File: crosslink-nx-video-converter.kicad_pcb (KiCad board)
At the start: 2 copper layers, 192 parts, among them J1 WE_68715014522, J2 WE_68715014522, J3 DC_SOCKET, J4 031-70526-21, J5 031-70526-21, U1 AP7330-W5-7, U10 GS2971A, U11 GS2988, U2 AP7330-W5-7, U3 AP7330-W5-7, U4 AP62301WU-7, U5 AP62301WU-7, U6 AP62301WU-7, U7 MT41K128M16JT-125_K, U8 NCV51200MNTXG, U9 LIFCL-40-9BG256C, Y1 ABM7_27.000MH_D2Y_T

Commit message: Made PCB mockup
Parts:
- removed F3, F4, F5: 04671.25NR, antmicro-footprints:0603-Fuse-Littelfuse-0467
- added C100: C_100n_0603, antmicro-footprints:0603-cap, F.Cu at (496.9, 90.8)
- added C101: C_100n_0603, antmicro-footprints:0603-cap, F.Cu at (493.3, 98.2)
- added C102: C_100n_0603, antmicro-footprints:0603-cap, F.Cu at (500.4, 90.8)
- added C103: C_100n_0603, antmicro-footprints:0603-cap, F.Cu at (493.3, 90.8)
- added C104: C_100n_0603, antmicro-footprints:0603-cap, F.Cu at (496.9, 85.8)
- added C105: C_100n_0603, antmicro-footprints:0603-cap, F.Cu at (489.8, 95.7)
- added C106: C_100n_0603, antmicro-footprints:0603-cap, F.Cu at (496.9, 93.2)
- added C94: C_100n_0603, antmicro-footprints:0603-cap, F.Cu at (452.4, 107.2)
- added C99: C_100n_0603, antmicro-footprints:0603-cap, F.Cu at (489.8, 88.3)
- added D1: LTST-C190GKT, antmicro-footprints:LED_0603, F.Cu at (322.0, 107.8)
- added D10: LTST-C190GKT, antmicro-footprints:LED_0603, F.Cu at (167.0, 59.0)
- added D11: LTST-C190GKT, antmicro-footprints:LED_0603, F.Cu at (153.0, 108.5)
- added D12: LTST-C190KRKT, antmicro-footprints:LED_0603, F.Cu at (156.0, 108.5)
- added D2: LTST-C190GKT, antmicro-footprints:LED_0603, F.Cu at (324.0, 107.8)
- added D3: LTST-C190GKT, antmicro-footprints:LED_0603, F.Cu at (326.0, 107.8)
- added D4: LTST-C190GKT, antmicro-footprints:LED_0603, F.Cu at (328.0, 107.8)
- added D5: LTST-C190GKT, antmicro-footprints:LED_0603, F.Cu at (330.0, 107.8)
- added D6: LTST-C190GKT, antmicro-footprints:LED_0603, F.Cu at (332.0, 107.8)
- added D7: LTST-C190GKT, antmicro-footprints:LED_0603, F.Cu at (334.0, 107.8)
- added D8: LTST-C190GKT, antmicro-footprints:LED_0603, F.Cu at (336.0, 107.8)
- added D9: LTST-C190GKT, antmicro-footprints:LED_0603, F.Cu at (164.0, 59.0)
- added G***: antmicro-logo_scaled_20mm, antmicro-footprints:antmicro-logo_scaled_20mm, F.Cu at (97.0, 60.0)
- added J6: FTSH-105-01-F-DV-K, antmicro-footprints:PinHeader_2x5_P1.27_SMD, F.Cu at (143.0, 61.0)
- added J7: FTSH-105-01-L-DV-K, antmicro-footprints:PinHeader_2x5_P1.27_SMD, F.Cu at (130.0, 110.0)
- added J8: 2X05, antmicro-footprints:SHF-105-01-X-D-SM, F.Cu at (143.5, 109.5)
- added Q1: 2N7002, antmicro-footprints:SOT-23-3, F.Cu at (374.3, 79.1)
- added Q10: 2N7002, antmicro-footprints:SOT-23-3, F.Cu at (386.7, 57.3)
- added Q11: 2N7002, antmicro-footprints:SOT-23-3, F.Cu at (391.4, 57.3)
- added Q12: 2N7002, antmicro-footprints:SOT-23-3, F.Cu at (376.7, 67.9)
- added Q13: 2N7002, antmicro-footprints:SOT-23-3, F.Cu at (378.3, 121.1)
- added Q2: AO3401A, antmicro-footprints:SOT-23-3, F.Cu at (369.6, 84.4)
- added Q3: AO3401A, antmicro-footprints:SOT-23-3, F.Cu at (381.4, 67.6)
- added Q4: 2N7002, antmicro-footprints:SOT-23-3, F.Cu at (386.1, 67.2)
- added Q5: 2N7002, antmicro-footprints:SOT-23-3, F.Cu at (391.4, 62.2)
- added Q6: AO3401A, antmicro-footprints:SOT-23-3, F.Cu at (396.1, 57.3)
- added Q7: 2N7002, antmicro-footprints:SOT-23-3, F.Cu at (386.7, 62.2)
- added Q8: 2N7002, antmicro-footprints:SOT-23-3, F.Cu at (381.4, 62.6)
- added Q9: 2N7002, antmicro-footprints:SOT-23-3, F.Cu at (381.4, 72.5)
- added R100: R_0R_0603, antmicro-footprints:0603-res, F.Cu at (412.6, 98.8)
- added R101: R_0R_0603, antmicro-footprints:0603-res, F.Cu at (402.0, 103.7)
- added R102: R_0R_0603, antmicro-footprints:0603-res, F.Cu at (412.6, 96.3)
- added R103: R_0R_0603, antmicro-footprints:0603-res, F.Cu at (394.9, 103.8)
- added R104: R_0R_0603, antmicro-footprints:0603-res, F.Cu at (405.5, 96.3)
- added R105: R_10k_0603, antmicro-footprints:0603-res, F.Cu at (397.6, 106.3)
- added R52: 4x51R_0402_array, antmicro-footprints:R_Array_4x0402, F.Cu at (353.0, 101.0)
- added R53: 4x51R_0402_array, antmicro-footprints:R_Array_4x0402, F.Cu at (353.0, 104.2)
- added R54: R_240R_1%_0402, antmicro-footprints:0402-res, F.Cu at (400.1, 67.7)
- added R55: R_75R_0402, antmicro-footprints:0402-res, F.Cu at (383.1, 85.5)
- added R56: R_75R_0402, antmicro-footprints:0402-res, F.Cu at (382.1, 90.4)
- added R57: R_37R4_0402, antmicro-footprints:0402-res, F.Cu at (393.1, 87.0)
- added R58: R_750R_0603, antmicro-footprints:0603-res, F.Cu at (392.0, 77.2)
- added R59: R_0R_0603, antmicro-footprints:0603-res, F.Cu at (379.1, 79.4)
- added R60: R_100k_0603, antmicro-footprints:0603-res, F.Cu at (407.1, 74.2)
- added R61: R_100k_0603, antmicro-footprints:0603-res, F.Cu at (399.1, 80.0)
- added R62: R_75R_0402, antmicro-footprints:0402-res, F.Cu at (409.1, 61.9)
- added R63: R_75R_0402, antmicro-footprints:0402-res, F.Cu at (400.1, 70.2)
- added R64: R_75R_0402, antmicro-footprints:0402-res, F.Cu at (408.8, 64.3)
- added R65: R_75R_0402, antmicro-footprints:0402-res, F.Cu at (452.7, 105.0)
- added R66: R_105R_0402, antmicro-footprints:0402-res, F.Cu at (449.1, 106.7)
- added R67: R_470R_0603, antmicro-footprints:0603-res, F.Cu at (452.0, 76.4)
- added R68: R_470R_0603, antmicro-footprints:0603-res, F.Cu at (448.5, 76.4)
- added R69: R_0R_0603, antmicro-footprints:0603-res, F.Cu at (389.6, 112.8)
- added R70: R_0R_0603, antmicro-footprints:0603-res, F.Cu at (389.6, 117.7)
- added R71: R_0R_0603, antmicro-footprints:0603-res, F.Cu at (404.7, 106.2)
- added R72: R_0R_0603, antmicro-footprints:0603-res, F.Cu at (386.0, 115.8)
- added R73: R_0R_0603, antmicro-footprints:0603-res, F.Cu at (402.0, 96.3)
- added R74: R_0R_0603, antmicro-footprints:0603-res, F.Cu at (367.5, 125.0)
- added R75: R_10k_0603, antmicro-footprints:0603-res, F.Cu at (396.6, 116.2)
- added R76: R_100R_0603, antmicro-footprints:0603-res, F.Cu at (401.1, 106.3)
- added R77: R_0R_0603, antmicro-footprints:0603-res, F.Cu at (385.9, 120.8)
- added R78: R_100R_0603, antmicro-footprints:0603-res, F.Cu at (409.1, 98.8)
- added R79: R_1k_0603, antmicro-footprints:0603-res, F.Cu at (408.2, 106.2)
- added R80: R_0R_0603, antmicro-footprints:0603-res, F.Cu at (388.4, 123.2)
- added R81: R_0R_0603, antmicro-footprints:0603-res, F.Cu at (396.6, 111.2)
- added R82: R_0R_0603, antmicro-footprints:0603-res, F.Cu at (377.7, 124.8)
- added R83: R_0R_0603, antmicro-footprints:0603-res, F.Cu at (393.1, 115.3)
- added R84: R_0R_0603, antmicro-footprints:0603-res, F.Cu at (402.0, 98.8)
- added R85: R_0R_0603, antmicro-footprints:0603-res, F.Cu at (405.6, 103.7)
- added R86: R_0R_0603, antmicro-footprints:0603-res, F.Cu at (389.6, 115.3)
- added R87: R_0R_0603, antmicro-footprints:0603-res, F.Cu at (409.1, 101.2)
- added R88: R_0R_0603, antmicro-footprints:0603-res, F.Cu at (405.6, 101.2)
- added R89: R_0R_0603, antmicro-footprints:0603-res, F.Cu at (409.1, 96.3)
- added R90: R_4k7_0603, antmicro-footprints:0603-res, F.Cu at (395.0, 108.8)
- added R91: R_10k_0603, antmicro-footprints:0603-res, F.Cu at (393.1, 117.7)
- added R92: R_0R_0603, antmicro-footprints:0603-res, F.Cu at (387.9, 110.3)
- added R93: R_4k7_0603, antmicro-footprints:0603-res, F.Cu at (402.1, 108.8)
- added R94: R_100R_0603, antmicro-footprints:0603-res, F.Cu at (384.8, 124.8)
- added R95: R_4k7_0603, antmicro-footprints:0603-res, F.Cu at (371.1, 125.0)
- added R96: R_2k2_0603, antmicro-footprints:0603-res, F.Cu at (398.5, 103.8)
- added R97: R_10k_0603, antmicro-footprints:0603-res, F.Cu at (416.2, 96.3)
- added R98: R_0R_0603, antmicro-footprints:0603-res, F.Cu at (393.1, 112.8)
- added R99: R_2k2_0603, antmicro-footprints:0603-res, F.Cu at (393.1, 120.2)
- added REF**: mounting-hole-2.7mm-M2.5-Pad, antmicro-footprints:mounting-hole-2.7mm-M2.5-Pad, F.Cu at (80.0, 60.0)
- added REF**: mounting-hole-2.7mm-M2.5-Pad, antmicro-footprints:mounting-hole-2.7mm-M2.5-Pad, F.Cu at (80.0, 110.0)
- added REF**: mounting-hole-2.7mm-M2.5-Pad, antmicro-footprints:mounting-hole-2.7mm-M2.5-Pad, F.Cu at (175.0, 60.0)
- added REF**: mounting-hole-2.7mm-M2.5-Pad, antmicro-footprints:mounting-hole-2.7mm-M2.5-Pad, F.Cu at (175.0, 110.0)
- added S1: B3U-3000PM, antmicro-footprints:B3U-3000P, F.Cu at (154.5, 113.0)
- added SW1: SW_DIP_x06, antmicro-footprints:SW_SPST_6_Slide_MCDHN-06F-T-V_P1.27mm, F.Cu at (156.6, 61.0)
- added TP13: TP, antmicro-footprints:TP-R-1.5, F.Cu at (416.2, 66.4)
- added TP14: TP, antmicro-footprints:TP-R-1.5, F.Cu at (413.7, 69.3)
- added TP15: TP, antmicro-footprints:TP-R-1.5, F.Cu at (444.5, 118.1)
- added TP16: TP, antmicro-footprints:TP-R-1.5, F.Cu at (405.1, 108.7)
- added TP17: TP, antmicro-footprints:TP-R-1.5, F.Cu at (415.7, 98.8)
- added TP18: TP, antmicro-footprints:TP-R-1.5, F.Cu at (399.7, 113.7)
- added TP19: TP, antmicro-footprints:TP-R-1.5, F.Cu at (403.2, 111.2)
- added TP20: TP, antmicro-footprints:TP-R-1.5, F.Cu at (374.2, 113.4)
- added TP21: TP, antmicro-footprints:TP-R-1.5, F.Cu at (412.2, 101.2)
- added TP22: TP, antmicro-footprints:TP-R-1.5, F.Cu at (387.8, 125.7)
- added TP23: TP, antmicro-footprints:TP-R-1.5, F.Cu at (374.1, 125.1)
- added U12: SC18IS602BIPW, antmicro-footprints:SC18IS602B, F.Cu at (128.0, 98.0)
- added U13: W25Q32JVSSIQ, antmicro-footprints:SOIC-8_W5.3mm, F.Cu at (118.0, 98.0)
- added Y2: OSC40M-3.3_S5, antmicro-footprints:OSC-4_5.0x3.2mm, F.Cu at (109.2, 83.5)
- C1, C4: value C_1u_0603 -> C_22u_0805; footprint antmicro-footprints:0603-cap -> antmicro-footprints:0805-cap
- C10, C11, C84, C85: value C_100n_0603 -> C_10u_0603
- C13, C14: value C_22u_0805 -> C_100n_0603; footprint antmicro-footprints:0805-cap -> antmicro-footprints:0603-cap
- C15, C16, C17: value C_22u_0805 -> C_1u_0603; footprint antmicro-footprints:0805-cap -> antmicro-footprints:0603-cap
- C2, C3, C5: value C_1u_0603 -> C_100n_0402; footprint antmicro-footprints:0603-cap -> antmicro-footprints:0402-cap
- C25, C26, C30, C31, C32: value C_100n_0402 -> C_22u_0805; footprint antmicro-footprints:0402-cap -> antmicro-footprints:0805-cap
- C27, C28: value C_100n_0402 -> C_1u_0603; footprint antmicro-footprints:0402-cap -> antmicro-footprints:0603-cap
- C29: value C_100n_0402 -> C_10u_0603; footprint antmicro-footprints:0402-cap -> antmicro-footprints:0603-cap
- C35, C36, C40, C41: value C_22u_0805 -> C_100n_0402; footprint antmicro-footprints:0805-cap -> antmicro-footprints:0402-cap
- C42: value C_100n_0603 -> C_100n_0402; footprint antmicro-footprints:0603-cap -> antmicro-footprints:0402-cap
- C43, C44: value C_100n_0603 -> C_33p_0603
- C45, C46, C49: value C_100n_0603 -> C_1u_0402; footprint antmicro-footprints:0603-cap -> antmicro-footprints:0402-cap
- C47: value C_100n_0603 -> C_47n_0603
- C48, C50: value C_100n_0603 -> C_470n_0603
- C51: value C_100n_0603 -> C_10n_0402; footprint antmicro-footprints:0603-cap -> antmicro-footprints:0402-cap
- C52, C53: value C_100n_0603 -> C_4u7_0402; footprint antmicro-footprints:0603-cap -> antmicro-footprints:0402-cap
- C56, C57, C58, C59, C60, C62: value C_10u_0603 -> C_100n_0603
- C6, C7: value C_10u_0603 -> C_22u_0805; footprint antmicro-footprints:0603-cap -> antmicro-footprints:0805-cap
- C61: value C_1u_0603 -> C_100n_0603
- C63: value C_100n_0603 -> C_33u_0603
- C71, C72: value C_1u_0402 -> C_100n_0603; footprint antmicro-footprints:0402-cap -> antmicro-footprints:0603-cap
- C86: value C_10n_0402 -> C_10u_0603; footprint antmicro-footprints:0402-cap -> antmicro-footprints:0603-cap
- C87, C88: value C_4u7_0402 -> C_10u_0603; footprint antmicro-footprints:0402-cap -> antmicro-footprints:0603-cap
- C89: value C_33p_0603 -> C_1u_0603
- C90: value C_33p_0603 -> C_10u_0603
- C91, C93: value C_470n_0603 -> C_100n_0603
- C92: value C_47n_0603 -> C_100n_0603
- C95: value C_33u_0603 -> C_100n_0603
- J1: value WE_68715014522 -> DC_SOCKET; footprint antmicro-footprints:WE_68715014522 -> antmicro-footprints:DC_SOCKET
- J2: value WE_68715014522 -> 031-70526-21; footprint antmicro-footprints:WE_68715014522 -> antmicro-footprints:BNC_Edge_Conn
- J3: value DC_SOCKET -> 031-70526-21; footprint antmicro-footprints:DC_SOCKET -> antmicro-footprints:BNC_Edge_Conn
- J4, J5: value 031-70526-21 -> WE_68715014522_ONE-SIDE; footprint antmicro-footprints:BNC_Edge_Conn -> antmicro-footprints:WE_68715014522_ONE-SIDE
- R1, R2: value R_0R_0603 -> R_0R_0805; footprint antmicro-footprints:0603-res -> antmicro-footprints:0805-res
- R10: value R_0R_0603 -> R_470R_0603
- R11: value R_0R_0603 -> R_10k_0603
- R12: value R_0R_0603 -> R_100k_0603
- R13, R15: value R_0R_0805 -> R_470R_0603; footprint antmicro-footprints:0805-res -> antmicro-footprints:0603-res
- R16: value R_33k_0603 -> R_470R_0603
- R17: value R_10k_0603 -> R_470R_0603
- R18: value R_3k01_1%_0603 -> R_470R_0603
- R19: value R_10k_1%_0603 -> R_470R_0603
- R20: value R_13k7_1%_0603 -> R_0R_0805; footprint antmicro-footprints:0603-res -> antmicro-footprints:0805-res
- R21: value R_20k_1%_0603 -> R_0R_0805; footprint antmicro-footprints:0603-res -> antmicro-footprints:0805-res
- R23, R24, R33, R34: value R_0R_0805 -> R_0R_0603; footprint antmicro-footprints:0805-res -> antmicro-footprints:0603-res
- R25: value R_100R_0402 -> R_0R_0603; footprint antmicro-footprints:0402-res -> antmicro-footprints:0603-res
- R26: value 4x51R_0402_array -> R_3k01_1%_0603; footprint antmicro-footprints:R_Array_4x0402 -> antmicro-footprints:0603-res
- R27: value 4x51R_0402_array -> R_10k_1%_0603; footprint antmicro-footprints:R_Array_4x0402 -> antmicro-footprints:0603-res
- R28: value 4x51R_0402_array -> R_13k7_1%_0603; footprint antmicro-footprints:R_Array_4x0402 -> antmicro-footprints:0603-res
- R29: value 4x51R_0402_array -> R_20k_1%_0603; footprint antmicro-footprints:R_Array_4x0402 -> antmicro-footprints:0603-res
- R3: value R_0R_0603 -> R_10k_1%_0603
- R30: value 4x51R_0402_array -> R_33k_0603; footprint antmicro-footprints:R_Array_4x0402 -> antmicro-footprints:0603-res
- R31: value 4x51R_0402_array -> R_10k_0603; footprint antmicro-footprints:R_Array_4x0402 -> antmicro-footprints:0603-res
- R32: value R_240R_1%_0402 -> R_0R_0603; footprint antmicro-footprints:0402-res -> antmicro-footprints:0603-res
- R35: value R_10k_1%_0603 -> R_3k01_1%_0603
- R37: value R_100k_0603 -> R_12k_0603
- R38: value R_0R_0603 -> R_24k_0603
- R39: value R_0R_0603 -> R_18k7_1%_0603
- R4: value R_3k01_1%_0603 -> R_10k_1%_0603
- R40: value R_0R_0603 -> R_15k_0603
- R42, R43: value R_75R_0402 -> R_0R_0603; footprint antmicro-footprints:0402-res -> antmicro-footprints:0603-res
- R44: value R_37R4_0402 -> R_0R_0805; footprint antmicro-footprints:0402-res -> antmicro-footprints:0805-res
- R45, R46: value R_75R_0402 -> R_0R_0805; footprint antmicro-footprints:0402-res -> antmicro-footprints:0805-res
- R47: value R_75R_0402 -> R_100R_0402
- R48: value R_75R_0402 -> 4x51R_0402_array; footprint antmicro-footprints:0402-res -> antmicro-footprints:R_Array_4x0402
- R49, R50: value R_100k_0603 -> 4x51R_0402_array; footprint antmicro-footprints:0603-res -> antmicro-footprints:R_Array_4x0402
- R5: value R_10k_1%_0603 -> R_100k_0603
- R51: value R_105R_0402 -> 4x51R_0402_array; footprint antmicro-footprints:0402-res -> antmicro-footprints:R_Array_4x0402
- R6: value R_12k_0603 -> R_0R_0805; footprint antmicro-footprints:0603-res -> antmicro-footprints:0805-res
- R7: value R_24k_0603 -> R_10k_0603
- R8: value R_18k7_1%_0603 -> R_470R_0603
- R9: value R_15k_0603 -> R_0R_0603
- U1: value AP7330-W5-7 -> NCV51200MNTXG; footprint antmicro-footprints:SOT-23-5 -> antmicro-footprints:DFN-10-1EP_3x3mm
- U11: value GS2988 -> LIFCL-40-9BG256C; footprint antmicro-footprints:QFN-16_EP_4x4_Pitch0.65mm -> antmicro-footprints:BGA-256_16x16_14.0x14.0mm
- U2, U3: value AP7330-W5-7 -> AP62301WU-7; footprint antmicro-footprints:SOT-23-5 -> antmicro-footprints:TSOT23-6
- U5, U6: value AP62301WU-7 -> AP7330-W5-7; footprint antmicro-footprints:TSOT23-6 -> antmicro-footprints:SOT-23-5
- U7: value MT41K128M16JT-125_K -> AP7330-W5-7; footprint antmicro-footprints:BGA80P96C6X16_800X1400X110 -> antmicro-footprints:SOT-23-5
- U8: value NCV51200MNTXG -> MT41K128M16JT-125_K; footprint antmicro-footprints:DFN-10-1EP_3x3mm -> antmicro-footprints:BGA80P96C6X16_800X1400X110
- U9: value LIFCL-40-9BG256C -> GS2988; footprint antmicro-footprints:BGA-256_16x16_14.0x14.0mm -> antmicro-footprints:QFN-16_EP_4x4_Pitch0.65mm
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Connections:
- C1 pad 1: +3V3 -> Net-(C1-Pad1)
- C10 pad 2: Net-(C10-Pad2) -> GND
- C11 pad 2: Net-(C11-Pad2) -> GND
- C13 pad 2: GND -> Net-(C13-Pad2)
- C14 pad 2: GND -> Net-(C14-Pad2)
- C15 pad 1: Net-(C15-Pad1) -> +3V3
- C16 pad 1: Net-(C14-Pad1) -> +3V3
- C17 pad 1: Net-(C15-Pad1) -> +3V3
- C18 pad 1: Net-(C13-Pad1) -> Net-(C18-Pad1)
- C19 pad 1: Net-(C14-Pad1) -> Net-(C19-Pad1)
- C2 pad 1: +3V3 -> Net-(C1-Pad1)
- C2 pad 2: GND -> Net-(C2-Pad2)
- C20 pad 1: Net-(C15-Pad1) -> Net-(C20-Pad1)
- C21 pad 1: Net-(C13-Pad1) -> Net-(C18-Pad1)
- C22 pad 1: Net-(C13-Pad1) -> Net-(C19-Pad1)
- C23 pad 1: Net-(C14-Pad1) -> Net-(C20-Pad1)
- C24 pad 1: Net-(C15-Pad1) -> Net-(C18-Pad1)
- C25 pad 1: +1V35 -> Net-(C19-Pad1)
- C26 pad 1: +1V35 -> Net-(C20-Pad1)
- C27 pad 1: +1V35 -> 1V0_Clean
- C28 pad 1: +1V35 -> +1V2
- C29 pad 1: +1V35 -> +1V8
- C3 pad 1: +3V3 -> Net-(C2-Pad2)
- C30 pad 1: +1V35 -> Net-(C18-Pad1)
- C31 pad 1: +1V35 -> Net-(C19-Pad1)
- C32 pad 1: +1V35 -> Net-(C20-Pad1)
- C33 pad 2: Vref -> GND
- C34 pad 1: Vref -> +1V35
- C35 pad 1: Net-(C35-Pad1) -> +1V35
- C36 pad 1: Net-(C36-Pad1) -> +1V35
- C37 pad 1: Net-(C35-Pad1) -> +1V35
- C37 pad 2: Net-(C37-Pad2) -> GND
- C38 pad 1: Net-(C37-Pad2) -> +1V35
- C39 pad 1: Vref -> +1V35
- C4 pad 1: 1V0_Clean -> Net-(C4-Pad1)
- C40 pad 1: Vtt -> +1V35
- C41 pad 1: Vtt -> +1V35
- C41 pad 2: GND -> Vref
- C42 pad 1: +1V35 -> Vref
- C42 pad 2: Vref -> GND
- C43 pad 1: Vref -> GND
- C43 pad 2: GND -> /SDI/XTAL1
- C44 pad 1: +1V35 -> GND
- C44 pad 2: Vref -> /SDI/XTAL2
- C45 pad 1: Vref -> Net-(C45-Pad1)
- C45 pad 2: GND -> /SDI/SDI_P
- C46 pad 1: +1V35 -> Net-(C46-Pad1)
- C46 pad 2: GND -> /SDI/SDI_N
- C47 pad 1: /FPGA/VCC_AUX -> Net-(C47-Pad1)
- C48 pad 1: /FPGA/VCC_AUX -> Net-(C48-Pad1)
- C49 pad 1: 1V0_Power -> GND
- C49 pad 2: GND -> Net-(C49-Pad2)
- C5 pad 1: +1V2 -> Vref
- C50 pad 1: /FPGA/VCC_AUX -> Net-(C48-Pad1)
- C50 pad 2: GND -> Net-(C50-Pad2)
- C51 pad 1: 1V0_Power -> GND
- C51 pad 2: GND -> +3V3
- C52 pad 1: /FPGA/VCC_AUX -> Net-(C52-Pad1)
- C52 pad 2: GND -> Net-(C52-Pad2)
- C53 pad 1: 1V0_Power -> Net-(C53-Pad1)
- C53 pad 2: GND -> Net-(C53-Pad2)
- C54 pad 1: /FPGA/VCC_AUX -> +3V3
- C55 pad 1: +1V35 -> +1V2
- C56 pad 1: 1V0_Power -> +3V3
- C57 pad 1: /FPGA/VCC_AUX -> +1V2
- C58 pad 1: /FPGA/VCC_AUXA -> +3V3
- C59 pad 1: /FPGA/VCC_DPHY -> +1V2
- C6 pad 1: +1V8 -> Vtt
- C60 pad 1: /FPGA/VCC_ADPHY -> +3V3
- C61 pad 1: /FPGA/VCC_PLLDPHY -> +1V2
- C62 pad 1: /FPGA/VCC_AUX -> +3V3
- C63 pad 1: /FPGA/VCC_AUXA -> Net-(C63-Pad1)
- C64 pad 1: /FPGA/VCC_DPHY -> +1V2
- C65 pad 1: /FPGA/VCC_ADPHY -> +3V3
- C66 pad 1: /FPGA/VCC_PLLDPHY -> +1V2
- C67 pad 1: /FPGA/VCC_AUXA -> +3V3
- C68 pad 1: /FPGA/VCC_DPHY -> +1V35
- C68 pad 2: GND -> Vref
- C69 pad 1: /FPGA/VCC_ADPHY -> Vref
- C7 pad 1: Net-(C7-Pad1) -> Vtt
- C70 pad 1: /FPGA/VCC_PLLDPHY -> +3V3
- C71 pad 1: Net-(C71-Pad1) -> +3V3
- C71 pad 2: /SDI/SDI_P -> GND
- C72 pad 1: Net-(C72-Pad1) -> +3V3
- C72 pad 2: /SDI/SDI_N -> GND
- C73 pad 1: +3V3 -> +1V35
- C74 pad 1: +1V2 -> +3V3
- C75 pad 1: +3V3 -> +1V2
- C76 pad 1: +1V2 -> +3V3
- C77 pad 1: +3V3 -> +1V35
- C78 pad 1: +1V2 -> +1V35
- C78 pad 2: GND -> Vref
- C79 pad 1: +3V3 -> Vref
- C8 pad 1: Net-(C8-Pad1) -> +5V
- C80 pad 1: +1V2 -> +3V3
- C81 pad 1: +3V3 -> Net-(C81-Pad1)
- C82 pad 1: +1V2 -> +3V3
- C84 pad 1: +1V2 -> 1V0_Power
- C85 pad 1: +3V3 -> /FPGA Power/VCC_AUX
- C86 pad 1: GND -> /FPGA Power/VCC_AUXA
- C86 pad 2: +3V3 -> GND
- C87 pad 1: Net-(C87-Pad1) -> /FPGA Power/VCC_DPHY
- C87 pad 2: Net-(C87-Pad2) -> GND
- C88 pad 1: Net-(C88-Pad1) -> /FPGA Power/VCC_ADPHY
- C88 pad 2: Net-(C88-Pad2) -> GND
- C89 pad 1: GND -> /FPGA Power/VCC_PLLDPHY
- C89 pad 2: /SDI/XTAL1 -> GND
- C90 pad 1: GND -> /FPGA Power/VCC_AUX
- C90 pad 2: /SDI/XTAL2 -> GND
- C91 pad 1: Net-(U10-PadG1) -> 1V0_Power
- C92 pad 1: Net-(U10-PadA2) -> /FPGA Power/VCC_AUX
- C93 pad 1: Net-(U10-PadG1) -> /FPGA Power/VCC_AUXA
- C93 pad 2: Net-(U10-PadF1) -> GND
- C95 pad 1: Net-(U10-PadA4) -> /FPGA Power/VCC_ADPHY
- C96 pad 1: +3V3 -> /FPGA Power/VCC_PLLDPHY
- C97 pad 1: +3V3 -> 1V0_Power
- C98 pad 1: +1V2 -> /FPGA Power/VCC_AUX
- F1 pad 1: Net-(F1-Pad1) -> /Peripherals/FFC1_5V
- F2 pad 1: +5V -> /Peripherals/FFC1_3V3
- F2 pad 2: Net-(J1-Pad49) -> +3V3
- FB1 pad 1: /FPGA/VCC_AUX -> /FPGA Power/VCC_AUX
- FB2 pad 1: /FPGA/VCC_AUXA -> /FPGA Power/VCC_AUXA
- FB3 pad 1: /FPGA/VCC_DPHY -> /FPGA Power/VCC_DPHY
- FB4 pad 1: /FPGA/VCC_ADPHY -> /FPGA Power/VCC_ADPHY
- FB5 pad 1: /FPGA/VCC_PLLDPHY -> /FPGA Power/VCC_PLLDPHY
- J1 pad 1: MIPI0_D3_N -> ALT_5V
- J1 pad 2: MIPI0_D3_P -> GND
- J1 pad 3: MIPI0_D2_N -> GND
- J2 pad 1: unconnected-(J2-Pad1) -> Net-(J2-Pad1)
- J2 pad 2: unconnected-(J2-Pad2) -> GND
- J3 pad 1: Net-(F1-Pad1) -> Net-(C53-Pad2)
- J4 pad 1: Net-(J4-Pad1) -> MIPI0_D3_N
- J4 pad 2: GND -> MIPI0_D3_P
- J5 pad 1: Net-(C88-Pad2) -> unconnected-(J5-Pad1)
- J5 pad 2: GND -> unconnected-(J5-Pad2)
- L1 pad 1: Net-(C11-Pad2) -> Net-(C12-Pad2)
- L1 pad 2: Net-(C14-Pad1) -> Net-(C18-Pad1)
- L2 pad 1: Net-(C12-Pad2) -> Net-(C13-Pad2)
- L2 pad 2: Net-(C15-Pad1) -> Net-(C19-Pad1)
- L3 pad 1: Net-(C10-Pad2) -> Net-(C14-Pad2)
- L3 pad 2: Net-(C13-Pad1) -> Net-(C20-Pad1)
- L4 pad 1: Net-(C71-Pad1) -> Net-(C45-Pad1)
- L4 pad 2: Net-(J4-Pad1) -> Net-(J2-Pad1)
- L5 pad 1: Net-(L5-Pad1) -> Net-(C53-Pad1)
- L5 pad 2: Net-(C88-Pad1) -> Net-(L5-Pad2)
- R1 pad 1: +3V3 -> +1V35
- R1 pad 2: Net-(R1-Pad2) -> Net-(C1-Pad1)
- R10 pad 1: Net-(R10-Pad1) -> Net-(D2-Pad1)
- R10 pad 2: 1V0_Clean -> +5V
- R11 pad 1: Net-(R11-Pad1) -> Net-(Q3-Pad1)
- R11 pad 2: +1V2 -> Net-(Q3-Pad2)
- R12 pad 1: Net-(R12-Pad1) -> /Power Supply/Vtt_PGOOD
- R12 pad 2: +1V8 -> Net-(C4-Pad1)
- R13 pad 1: +5V -> Net-(D3-Pad1)
- R13 pad 2: Net-(C7-Pad1) -> +5V
- R14 pad 1: +5V -> Net-(Q2-Pad2)
- R14 pad 2: Net-(C8-Pad1) -> +5V
- R15 pad 1: +5V -> Net-(D4-Pad1)
- R15 pad 2: Net-(C9-Pad1) -> +5V
- R16 pad 1: Net-(C13-Pad1) -> Net-(D5-Pad1)
- R16 pad 2: Net-(R16-Pad2) -> +5V
- R17 pad 1: GND -> Net-(D6-Pad1)
- R17 pad 2: Net-(R16-Pad2) -> +5V
- R18 pad 1: Net-(C14-Pad1) -> Net-(D7-Pad1)
- R18 pad 2: Net-(R18-Pad2) -> +5V
- R19 pad 1: Net-(R18-Pad2) -> Net-(D8-Pad1)
- R19 pad 2: GND -> +5V
- R2 pad 1: +3V3 -> FFC2_5V
- R2 pad 2: Net-(R2-Pad2) -> Net-(Q3-Pad3)
- R20 pad 1: Net-(R20-Pad1) -> +5V
- R20 pad 2: Net-(C15-Pad1) -> Net-(C9-Pad1)
- R21 pad 1: GND -> +5V
- R21 pad 2: Net-(R20-Pad1) -> Net-(C10-Pad1)
- R22 pad 1: Net-(C13-Pad1) -> +5V
- R22 pad 2: +3V3 -> Net-(C11-Pad1)
- R23 pad 1: Net-(C14-Pad1) -> +3V3
- R23 pad 2: 1V0_Power -> Net-(R23-Pad2)
- R24 pad 1: Net-(C15-Pad1) -> +3V3
- R24 pad 2: +1V35 -> Net-(R24-Pad2)
- R25 pad 1: DDR3_CK_N -> +3V3
- R25 pad 2: DDR3_CK_P -> Net-(R25-Pad2)
- R26 pad 1: DDR3_A0 -> Net-(C18-Pad1)
- R26 pad 2: DDR3_A1 -> Net-(R26-Pad2)
- R27 pad 1: DDR3_A4 -> Net-(R26-Pad2)
- R27 pad 2: DDR3_A5 -> GND
- R28 pad 1: DDR3_A8 -> Net-(R28-Pad1)
- R28 pad 2: DDR3_A9 -> Net-(C19-Pad1)
- R29 pad 1: DDR3_A12 -> GND
- R29 pad 2: DDR3_A13 -> Net-(R28-Pad1)
- R3 pad 1: +3V3 -> Net-(C2-Pad2)
- R3 pad 2: Net-(R3-Pad2) -> Net-(C1-Pad1)
- R30 pad 1: ~{DDR3_RESET} -> Net-(C20-Pad1)
- R30 pad 2: ~{DDR3_RAS} -> Net-(R30-Pad2)
- R31 pad 1: ~{DDR3_CS} -> GND
- R31 pad 2: DDR3_ODT -> Net-(R30-Pad2)
- R32 pad 1: GND -> Net-(R23-Pad2)
- R33 pad 1: +1V35 -> Net-(R24-Pad2)
- R33 pad 2: Net-(C35-Pad1) -> Net-(R33-Pad2)
- R34 pad 1: +3V3 -> Net-(R25-Pad2)
- R34 pad 2: Net-(C36-Pad1) -> Net-(R34-Pad2)
- R35 pad 1: Net-(C37-Pad2) -> Net-(R35-Pad1)
- R35 pad 2: Net-(C35-Pad1) -> Net-(R35-Pad2)
- R36 pad 1: GND -> Net-(R35-Pad2)
- R36 pad 2: Net-(C37-Pad2) -> GND
- R37 pad 2: Net-(C36-Pad1) -> Net-(R37-Pad2)
- R38 pad 1: Net-(C35-Pad1) -> GND
- R38 pad 2: Net-(U8-Pad7) -> Net-(R37-Pad2)
- R39 pad 1: Net-(R1-Pad2) -> Net-(R39-Pad1)
- R39 pad 2: Net-(U1-Pad3) -> Net-(R39-Pad2)
- R4 pad 1: Net-(R10-Pad1) -> GND
- R4 pad 2: Net-(R4-Pad2) -> Net-(C2-Pad2)
- R40 pad 1: Net-(R2-Pad2) -> GND
- R40 pad 2: Net-(U2-Pad3) -> Net-(R39-Pad1)
- R41 pad 1: Net-(R3-Pad2) -> Net-(R35-Pad1)
- R41 pad 2: Net-(U3-Pad3) -> 1V0_Clean
- R42 pad 1: Net-(J4-Pad1) -> Net-(R37-Pad1)
- R42 pad 2: Net-(C71-Pad1) -> +1V2
- R43 pad 1: GND -> Net-(R39-Pad2)
- R43 pad 2: Net-(C71-Pad1) -> +1V8
- R44 pad 1: GND -> Net-(C20-Pad1)
- R44 pad 2: Net-(C72-Pad1) -> +3V3
- R45 pad 1: +3V3 -> Net-(C18-Pad1)
- R45 pad 2: Net-(L5-Pad1) -> 1V0_Power
- R46 pad 1: Net-(C87-Pad1) -> Net-(C19-Pad1)
- R46 pad 2: +3V3 -> +1V35
- R47 pad 1: Net-(L5-Pad1) -> DDR3_CK_N
- R47 pad 2: Net-(C88-Pad1) -> DDR3_CK_P
- R48 pad 1: Net-(C87-Pad2) -> DDR3_A0
- R48 pad 2: GND -> DDR3_A1
- R49 pad 1: GND -> DDR3_A4
- R49 pad 2: Net-(U10-PadA3) -> DDR3_A5
- R5 pad 1: Net-(R4-Pad2) -> GND
- R5 pad 2: GND -> ALT_5V
- R50 pad 1: Net-(U10-PadA3) -> DDR3_A8
- R50 pad 2: +3V3 -> DDR3_A9
- R51 pad 1: +1V2 -> DDR3_A12
- R51 pad 2: Net-(U10-PadA4) -> DDR3_A13
- R6 pad 1: Net-(R11-Pad1) -> +3V3
- R6 pad 2: Net-(R6-Pad2) -> Net-(C4-Pad1)
- R7 pad 1: GND -> Net-(Q1-Pad3)
- R7 pad 2: Net-(R6-Pad2) -> Net-(Q3-Pad3)
- R8 pad 1: Net-(R8-Pad1) -> Net-(D1-Pad1)
- R8 pad 2: Net-(R12-Pad1) -> +5V
- R9 pad 1: GND -> Net-(C1-Pad1)
- R9 pad 2: Net-(R8-Pad1) -> Net-(R9-Pad2)
- TP1 pad 1: Net-(U5-Pad5) -> GND
- TP10 pad 1: +1V35 -> /Power Supply/Vtt_PGOOD
- TP11 pad 1: +1V2 -> Net-(TP11-Pad1)
- TP12 pad 1: Net-(U10-PadH6) -> Net-(TP12-Pad1)
- TP2 pad 1: Net-(R37-Pad1) -> +5V
- TP3 pad 1: Net-(U6-Pad5) -> +3V3
- TP4 pad 1: Net-(U4-Pad5) -> 1V0_Power
- TP5 pad 1: +5V -> 1V0_Clean
- TP6 pad 1: +3V3 -> +1V8
- TP7 pad 1: 1V0_Power -> +1V35
- TP8 pad 1: 1V0_Clean -> +1V2
- TP9 pad 1: +1V8 -> GND
- U1 pad 1: Net-(R1-Pad2) -> Net-(C2-Pad2)
- U1 pad 2: GND -> Net-(C1-Pad1)
- U1 pad 3: Net-(U1-Pad3) -> Vtt
- U1 pad 4: Net-(R4-Pad2) -> GND
- U1 pad 5: Net-(R10-Pad1) -> Vtt
- U10 pad A1: Net-(U10-PadA1) -> Net-(C49-Pad2)
- U10 pad A2: Net-(U10-PadA2) -> Net-(C47-Pad1)
- U10 pad A3: Net-(U10-PadA3) -> Net-(R60-Pad2)
- U10 pad A4: Net-(U10-PadA4) -> Net-(C63-Pad1)
- U10 pad C7: unconnected-(U10-PadC7) -> RESET_TRST
- U10 pad D7: unconnected-(U10-PadD7) -> SW_EN
- U10 pad D8: unconnected-(U10-PadD8) -> JTAG/~{HOST}
- U10 pad E7: unconnected-(U10-PadE7) -> SDOUT_TDO
- U10 pad E8: unconnected-(U10-PadE8) -> SDIN_TDI
- U10 pad F1: Net-(U10-PadF1) -> Net-(C50-Pad2)
- U10 pad F7: unconnected-(U10-PadF7) -> ~{CS_TMS}
- U10 pad F8: unconnected-(U10-PadF8) -> SCLK_TCK
- U10 pad G1: Net-(U10-PadG1) -> Net-(C48-Pad1)
- U10 pad G3: unconnected-(U10-PadG3) -> ~{RC_BYP}
- U10 pad G7: unconnected-(U10-PadG7) -> ~{SMPTE_BYPASS}
- U10 pad G8: unconnected-(U10-PadG8) -> DVB_ASI
- U10 pad H3: unconnected-(U10-PadH3) -> AUDIO_EN/~{DIS}
- U10 pad H4: unconnected-(U10-PadH4) -> AUDIO_WCLK
- U10 pad H5: unconnected-(U10-PadH5) -> TIM_861
- U10 pad H6: Net-(U10-PadH6) -> Net-(TP14-Pad1)
- U10 pad H7: unconnected-(U10-PadH7) -> 20bit/~{10bit}
- U10 pad H8: unconnected-(U10-PadH8) -> IOPROC_EN/~{DIS}
- U10 pad J1: unconnected-(U10-PadJ1) -> /SDI/SDO_P
- U10 pad J2: unconnected-(U10-PadJ2) -> SDO_EN/DIS
- U10 pad J3: unconnected-(U10-PadJ3) -> AUDIO_OUT_CH1_2
- U10 pad J4: unconnected-(U10-PadJ4) -> AUDIO_ACLK
- U10 pad J5: unconnected-(U10-PadJ5) -> AUDIO_OUT_CH5_6
- U10 pad K1: unconnected-(U10-PadK1) -> /SDI/SDO_N
- U10 pad K2: unconnected-(U10-PadK2) -> STANDBY
- U10 pad K3: unconnected-(U10-PadK3) -> AUDIO_OUT_CH3_4
- U10 pad K4: unconnected-(U10-PadK4) -> AUDIO_MCLK
- U10 pad K5: unconnected-(U10-PadK5) -> AUDIO_OUT_CH7_8
- U2 pad 1: Net-(R2-Pad2) -> GND
- U2 pad 2: GND -> Net-(C12-Pad2)
- U2 pad 3: Net-(U2-Pad3) -> Net-(C9-Pad1)
- U2 pad 4: Net-(R6-Pad2) -> Net-(R26-Pad2)
- U2 pad 5: Net-(R11-Pad1) -> Net-(TP11-Pad1)
- U3 pad 1: Net-(R3-Pad2) -> GND
- U3 pad 2: GND -> Net-(C13-Pad2)
- U3 pad 3: Net-(U3-Pad3) -> Net-(C10-Pad1)
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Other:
- board outline added: 105.7 x 60 mm
- board text added: "CROSSLINK NX VIDEO CONVERTER"

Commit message: Added loclib
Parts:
- C1, C18, C19, C20, C21, C22, C23, C24, C25, C26, C30, C31, C32, C4, C6, C7: footprint antmicro-footprints:0805-cap -> crosslink-nx-video-converter-footprints:0805-cap
- C10, C100, C101, C102, C103, C104, C105, C106, C11, C12, C13, C14, C15, C16, C17, C27, C28, C29, C43, C44, C47, C48, C50, C54, C55, C56, C57, C58, C59, C60, C61, C62, C63, C64, C65, C66, C67, C68, C69, C70, C71, C72, C73, C74, C75, C76, C77, C78, C79, C8, C80, C81, C82, C83, C84, C85, C86, C87, C88, C89, C9, C90, C91, C92, C93, C94, C95, C96, C97, C98, C99: footprint antmicro-footprints:0603-cap -> crosslink-nx-video-converter-footprints:0603-cap
- C2, C3, C33, C34, C35, C36, C37, C38, C39, C40, C41, C42, C45, C46, C49, C5, C51, C52, C53, L4, L5: footprint antmicro-footprints:0402-cap -> crosslink-nx-video-converter-footprints:0402-cap
- D1, D10, D11, D12, D2, D3, D4, D5, D6, D7, D8, D9: footprint antmicro-footprints:LED_0603 -> crosslink-nx-video-converter-footprints:LED_0603
- F1, F2: footprint antmicro-footprints:0603-Fuse-Littelfuse-0467 -> crosslink-nx-video-converter-footprints:0603-Fuse-Littelfuse-0467
- FB1, FB2, FB3, FB4, FB5, R10, R100, R101, R102, R103, R104, R105, R11, R12, R13, R15, R16, R17, R18, R19, R23, R24, R25, R26, R27, R28, R29, R3, R30, R31, R32, R33, R34, R35, R36, R37, R38, R39, R4, R40, R41, R42, R43, R5, R58, R59, R60, R61, R67, R68, R69, R7, R70, R71, R72, R73, R74, R75, R76, R77, R78, R79, R8, R80, R81, R82, R83, R84, R85, R86, R87, R88, R89, R9, R90, R91, R92, R93, R94, R95, R96, R97, R98, R99: footprint antmicro-footprints:0603-res -> crosslink-nx-video-converter-footprints:0603-res
- G***: footprint antmicro-footprints:antmicro-logo_scaled_20mm -> crosslink-nx-video-converter-footprints:antmicro-logo_scaled_20mm
- J1: footprint antmicro-footprints:DC_SOCKET -> crosslink-nx-video-converter-footprints:DC_SOCKET
- J2, J3: footprint antmicro-footprints:BNC_Edge_Conn -> crosslink-nx-video-converter-footprints:BNC_Edge_Conn
- J4, J5: footprint antmicro-footprints:WE_68715014522_ONE-SIDE -> crosslink-nx-video-converter-footprints:WE_68715014522_ONE-SIDE
- J6, J7: footprint antmicro-footprints:PinHeader_2x5_P1.27_SMD -> crosslink-nx-video-converter-footprints:PinHeader_2x5_P1.27_SMD
- J8: footprint antmicro-footprints:SHF-105-01-X-D-SM -> crosslink-nx-video-converter-footprints:SHF-105-01-X-D-SM
- L1, L2, L3: footprint antmicro-footprints:Coilcraft-XEL4030 -> crosslink-nx-video-converter-footprints:Coilcraft-XEL4030
- Q1, Q10, Q11, Q12, Q13, Q2, Q3, Q4, Q5, Q6, Q7, Q8, Q9: footprint antmicro-footprints:SOT-23-3 -> crosslink-nx-video-converter-footprints:SOT-23-3
- R1, R14, R2, R20, R21, R22, R44, R45, R46, R6: footprint antmicro-footprints:0805-res -> crosslink-nx-video-converter-footprints:0805-res
- R47, R54, R55, R56, R57, R62, R63, R64, R65, R66: footprint antmicro-footprints:0402-res -> crosslink-nx-video-converter-footprints:0402-res
- R48, R49, R50, R51, R52, R53: footprint antmicro-footprints:R_Array_4x0402 -> crosslink-nx-video-converter-footprints:R_Array_4x0402
- REF** (x4): footprint antmicro-footprints:mounting-hole-2.7mm-M2.5-Pad -> crosslink-nx-video-converter-footprints:mounting-hole-2.7mm-M2.5-Pad
- S1: footprint antmicro-footprints:B3U-3000P -> crosslink-nx-video-converter-footprints:B3U-3000P
- SW1: footprint antmicro-footprints:SW_SPST_6_Slide_MCDHN-06F-T-V_P1.27mm -> crosslink-nx-video-converter-footprints:SW_SPST_6_Slide_MCDHN-06F-T-V_P1.27mm
- TP1, TP10, TP11, TP12, TP13, TP14, TP15, TP16, TP17, TP18, TP19, TP2, TP20, TP21, TP22, TP23, TP3, TP4, TP5, TP6, TP7, TP8, TP9: footprint antmicro-footprints:TP-R-1.5 -> crosslink-nx-video-converter-footprints:TP-R-1.5
- U1: footprint antmicro-footprints:DFN-10-1EP_3x3mm -> crosslink-nx-video-converter-footprints:DFN-10-1EP_3x3mm
- U10: footprint antmicro-footprints:BGA100_11x11mm -> crosslink-nx-video-converter-footprints:BGA100_11x11mm
- U11: footprint antmicro-footprints:BGA-256_16x16_14.0x14.0mm -> crosslink-nx-video-converter-footprints:BGA-256_16x16_14.0x14.0mm
- U12: footprint antmicro-footprints:SC18IS602B -> crosslink-nx-video-converter-footprints:SC18IS602B
- U13: footprint antmicro-footprints:SOIC-8_W5.3mm -> crosslink-nx-video-converter-footprints:SOIC-8_W5.3mm
- U2, U3, U4: footprint antmicro-footprints:TSOT23-6 -> crosslink-nx-video-converter-footprints:TSOT23-6
- U5, U6, U7: footprint antmicro-footprints:SOT-23-5 -> crosslink-nx-video-converter-footprints:SOT-23-5
- U8: footprint antmicro-footprints:BGA80P96C6X16_800X1400X110 -> crosslink-nx-video-converter-footprints:BGA80P96C6X16_800X1400X110
- U9: footprint antmicro-footprints:QFN-16_EP_4x4_Pitch0.65mm -> crosslink-nx-video-converter-footprints:QFN-16_EP_4x4_Pitch0.65mm
- Y1: footprint antmicro-footprints:ABM7_OSC -> crosslink-nx-video-converter-footprints:ABM7_OSC
- Y2: footprint antmicro-footprints:OSC-4_5.0x3.2mm -> crosslink-nx-video-converter-footprints:OSC-4_5.0x3.2mm

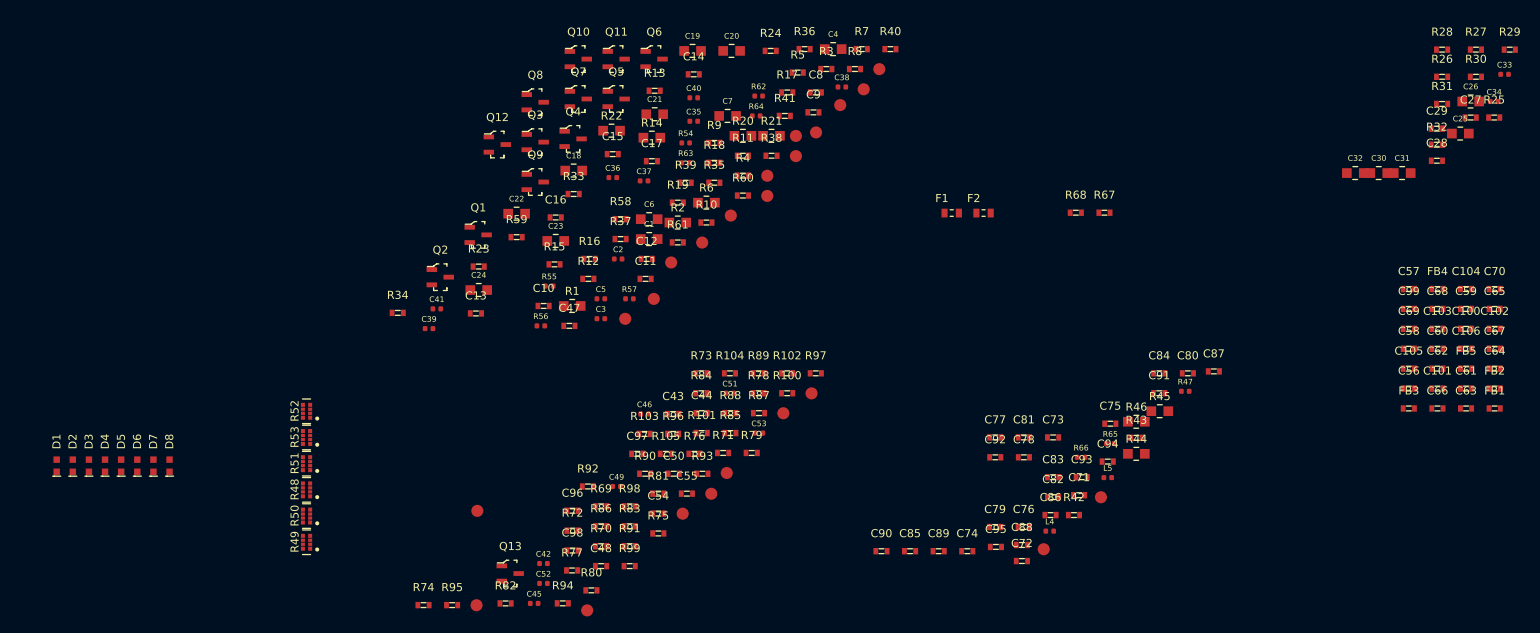
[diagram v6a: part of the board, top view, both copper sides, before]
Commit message: Removed components outside PCB
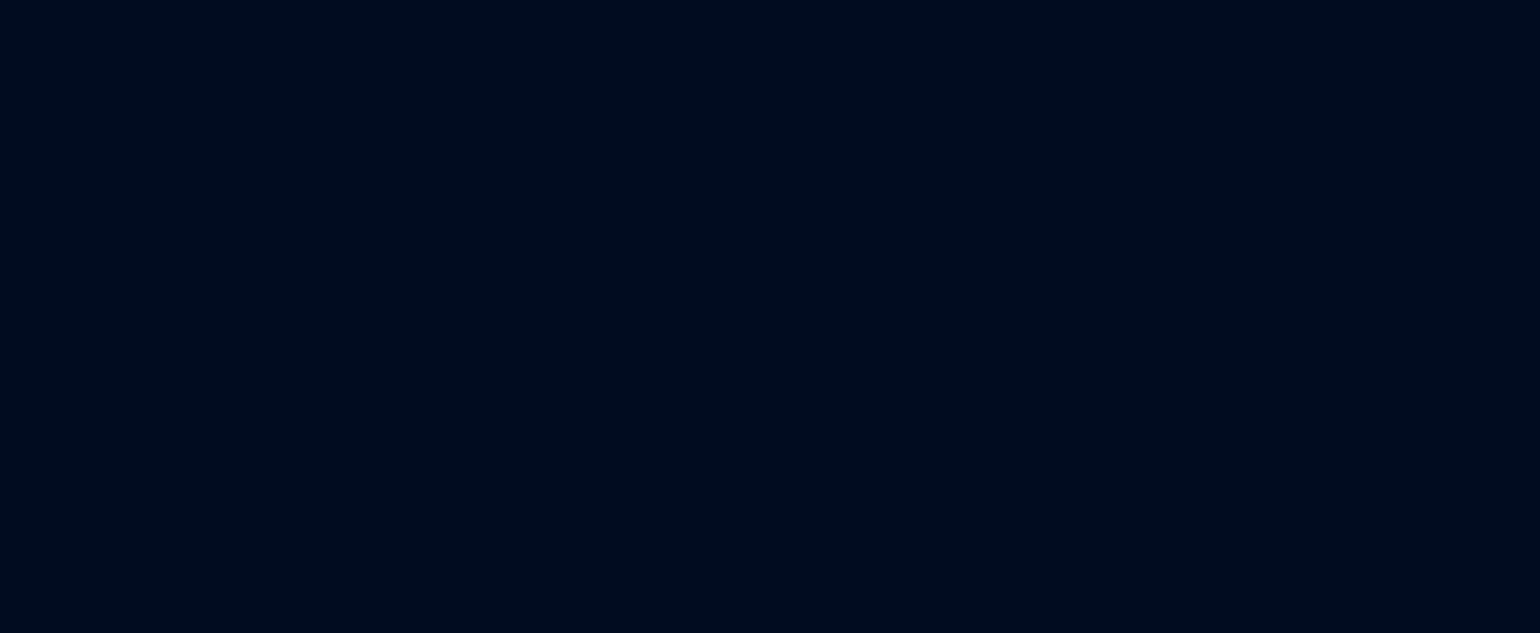
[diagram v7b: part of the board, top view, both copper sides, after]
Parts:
- removed C1, C18, C19, C20, C21, C22, C23, C24, C25, C26, C30, C31, C32, C4, C6, C7: C_22u_0805, crosslink-nx-video-converter-footprints:0805-cap
- removed C10, C11, C29, C8, C84, C85, C86, C87, C88, C9, C90: C_10u_0603, crosslink-nx-video-converter-footprints:0603-cap
- removed C100, C101, C102, C103, C104, C105, C106, C12, C13, C14, C54, C55, C56, C57, C58, C59, C60, C61, C62, C64, C65, C66, C67, C68, C69, C70, C71, C72, C73, C74, C75, C76, C77, C78, C79, C80, C81, C82, C83, C91, C92, C93, C94, C95, C96, C97, C98, C99: C_100n_0603, crosslink-nx-video-converter-footprints:0603-cap
- removed C15, C16, C17, C27, C28, C89: C_1u_0603, crosslink-nx-video-converter-footprints:0603-cap
- removed C2, C3, C33, C34, C35, C36, C37, C38, C39, C40, C41, C42, C5: C_100n_0402, crosslink-nx-video-converter-footprints:0402-cap
- removed C43, C44: C_33p_0603, crosslink-nx-video-converter-footprints:0603-cap
- removed C45, C46, C49: C_1u_0402, crosslink-nx-video-converter-footprints:0402-cap
- removed C47: C_47n_0603, crosslink-nx-video-converter-footprints:0603-cap
- removed C48, C50: C_470n_0603, crosslink-nx-video-converter-footprints:0603-cap
- removed C51: C_10n_0402, crosslink-nx-video-converter-footprints:0402-cap
- removed C52, C53: C_4u7_0402, crosslink-nx-video-converter-footprints:0402-cap
- removed C63: C_33u_0603, crosslink-nx-video-converter-footprints:0603-cap
- removed D1, D2, D3, D4, D5, D6, D7, D8: LTST-C190GKT, crosslink-nx-video-converter-footprints:LED_0603
- removed F1, F2: 04671.25NR, crosslink-nx-video-converter-footprints:0603-Fuse-Littelfuse-0467
- removed FB1, FB2, FB3, FB4, FB5: BLM18PG121SN1D, crosslink-nx-video-converter-footprints:0603-res
- removed L4, L5: L_0402_6n2, crosslink-nx-video-converter-footprints:0402-cap
- removed Q1, Q10, Q11, Q12, Q13, Q4, Q5, Q7, Q8, Q9: 2N7002, crosslink-nx-video-converter-footprints:SOT-23-3
- removed Q2, Q3, Q6: AO3401A, crosslink-nx-video-converter-footprints:SOT-23-3
- removed R1, R14, R2, R20, R21, R22, R44, R45, R46, R6: R_0R_0805, crosslink-nx-video-converter-footprints:0805-res
- removed R10, R13, R15, R16, R17, R18, R19, R67, R68, R8: R_470R_0603, crosslink-nx-video-converter-footprints:0603-res
- removed R100, R101, R102, R103, R104, R23, R24, R25, R32, R33, R34, R41, R42, R43, R59, R69, R70, R71, R72, R73, R74, R77, R80, R81, R82, R83, R84, R85, R86, R87, R88, R89, R9, R92, R98: R_0R_0603, crosslink-nx-video-converter-footprints:0603-res
- removed R105, R11, R31, R7, R75, R91, R97: R_10k_0603, crosslink-nx-video-converter-footprints:0603-res
- removed R12, R5, R60, R61: R_100k_0603, crosslink-nx-video-converter-footprints:0603-res
- removed R26, R35: R_3k01_1%_0603, crosslink-nx-video-converter-footprints:0603-res
- removed R27, R3, R36, R4: R_10k_1%_0603, crosslink-nx-video-converter-footprints:0603-res
- removed R28: R_13k7_1%_0603, crosslink-nx-video-converter-footprints:0603-res
- removed R29: R_20k_1%_0603, crosslink-nx-video-converter-footprints:0603-res
- removed R30: R_33k_0603, crosslink-nx-video-converter-footprints:0603-res
- removed R37: R_12k_0603, crosslink-nx-video-converter-footprints:0603-res
- removed R38: R_24k_0603, crosslink-nx-video-converter-footprints:0603-res
- removed R39: R_18k7_1%_0603, crosslink-nx-video-converter-footprints:0603-res
- removed R40: R_15k_0603, crosslink-nx-video-converter-footprints:0603-res
- removed R47: R_100R_0402, crosslink-nx-video-converter-footprints:0402-res
- removed R48, R49, R50, R51, R52, R53: 4x51R_0402_array, crosslink-nx-video-converter-footprints:R_Array_4x0402
- removed R54: R_240R_1%_0402, crosslink-nx-video-converter-footprints:0402-res
- removed R55, R56, R62, R63, R64, R65: R_75R_0402, crosslink-nx-video-converter-footprints:0402-res
- removed R57: R_37R4_0402, crosslink-nx-video-converter-footprints:0402-res
- removed R58: R_750R_0603, crosslink-nx-video-converter-footprints:0603-res
- removed R66: R_105R_0402, crosslink-nx-video-converter-footprints:0402-res
- removed R76, R78, R94: R_100R_0603, crosslink-nx-video-converter-footprints:0603-res
- removed R79: R_1k_0603, crosslink-nx-video-converter-footprints:0603-res
- removed R90, R93, R95: R_4k7_0603, crosslink-nx-video-converter-footprints:0603-res
- removed R96, R99: R_2k2_0603, crosslink-nx-video-converter-footprints:0603-res
- removed TP1, TP10, TP11, TP12, TP13, TP14, TP15, TP16, TP17, TP18, TP19, TP2, TP20, TP21, TP22, TP23, TP3, TP4, TP5, TP6, TP7, TP8, TP9: TP, crosslink-nx-video-converter-footprints:TP-R-1.5
